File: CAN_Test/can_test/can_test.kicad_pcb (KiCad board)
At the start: 4 copper layers, 30.6 x 40.6 mm, 8 parts, among them IC1 TCAN3414DR, IC2 TCAN3414DR, J1 Conn_01x04_Pin, U1 Teensy4.0

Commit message: final thing we ordered
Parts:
- added G***: LOGO, footprints:Logo_Small, B.Cu at (41.8, 35.2)
- added G***: LOGO, footprints:bird, B.Cu at (57.5, 33.7)

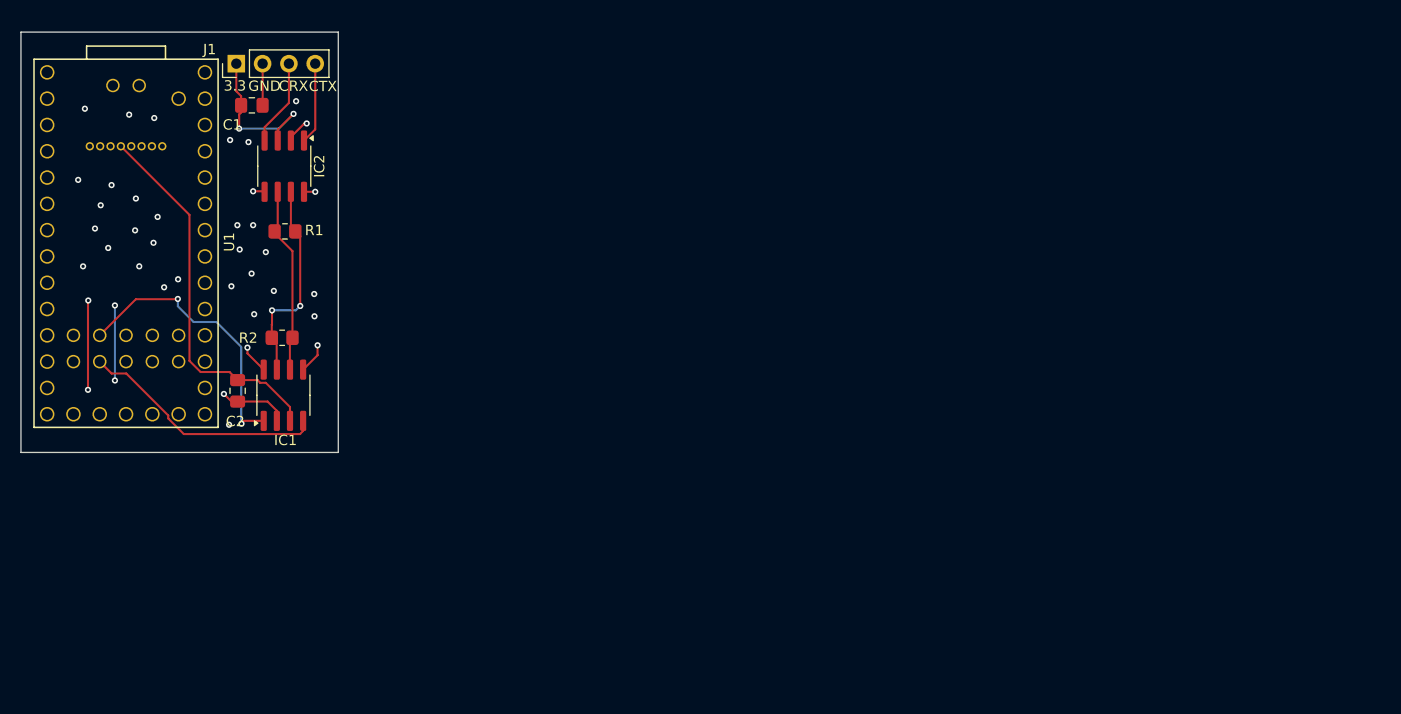
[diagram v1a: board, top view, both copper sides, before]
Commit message: update can test to teensy 41
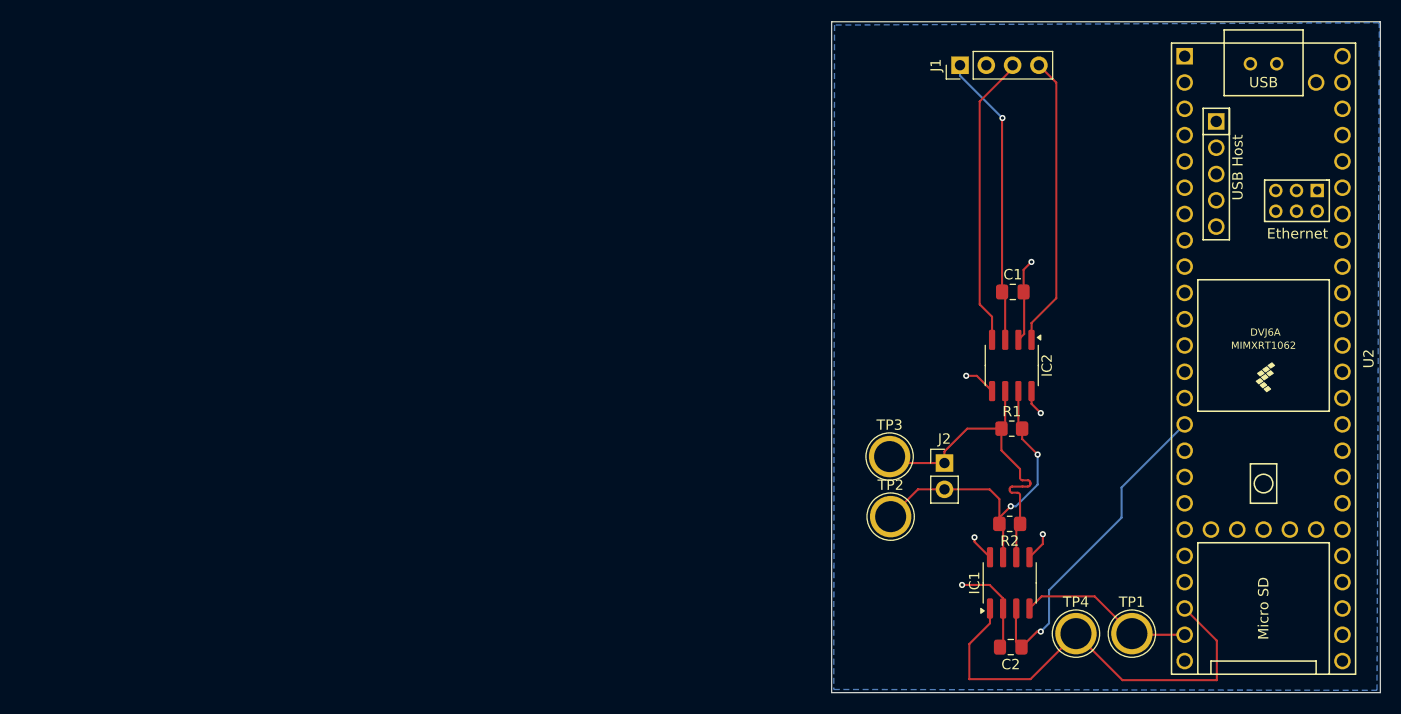
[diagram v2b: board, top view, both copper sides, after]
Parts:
- removed G***: LOGO, footprints:Logo_Small
- removed G***: LOGO, footprints:bird
- removed U1: Teensy4.0, teensy:Teensy40_SMT
- added J2: Conn_01x02_Pin, Connector_PinHeader_2.54mm:PinHeader_1x02_P2.54mm_Vertical, F.Cu at (121.3, 57.5)
- added TP1: TestPoint_Probe, TestPoint:TestPoint_Plated_Hole_D3.0mm, F.Cu at (139.4, 74.0)
- added TP2: TestPoint_Probe, TestPoint:TestPoint_Plated_Hole_D3.0mm, F.Cu at (116.1, 62.7)
- added TP3: TestPoint_Probe, TestPoint:TestPoint_Plated_Hole_D3.0mm, F.Cu at (116.0, 56.9)
- added TP4: TestPoint_Probe, TestPoint:TestPoint_Plated_Hole_D3.0mm, F.Cu at (134.0, 74.0)
- added U2: Teensy4.1, teensy:Teensy41, F.Cu at (152.1, 47.4)
- moved C2 78.7 mm to (127.7, 75.3), turned to 180 degrees
- moved C1 75.7 mm to (127.9, 41.0)
- moved IC2 72.9 mm to (127.8, 48.1)
- moved R1 72.7 mm to (127.8, 54.2)
- moved R2 72.5 mm to (127.6, 63.4)
- moved IC1 72.5 mm to (127.6, 69.1)
- moved J1 69.9 mm to (122.8, 19.1)
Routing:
- net CRX2: track 8.40 -> 28.8 mm
- net CTX2: track 7.88 -> 28.2 mm
- net CTX1: track 27.1 -> 43.5 mm, vias 2 -> 0
- net CANL: track 18.1 -> 33.5 mm
- net CANH: track 20.2 -> 33.2 mm
- net Net-(IC2-VCC): track 15.6 -> 28.4 mm, vias 2 -> 1
- net GND: track 37.0 -> 28.3 mm, vias 40 -> 6
- net CRX1: track 23.8 -> 17.0 mm
- net +3.3V: track 36.4 -> 32.2 mm, vias 0 -> 1
- added copper zone on B.Cu, net GND
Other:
- board size 30.6 x 40.6 mm -> 53 x 64.8 mm
- board text removed: "3.3"
- board text removed: "CRX"
- board text removed: "CTX"
- board text removed: "GND"

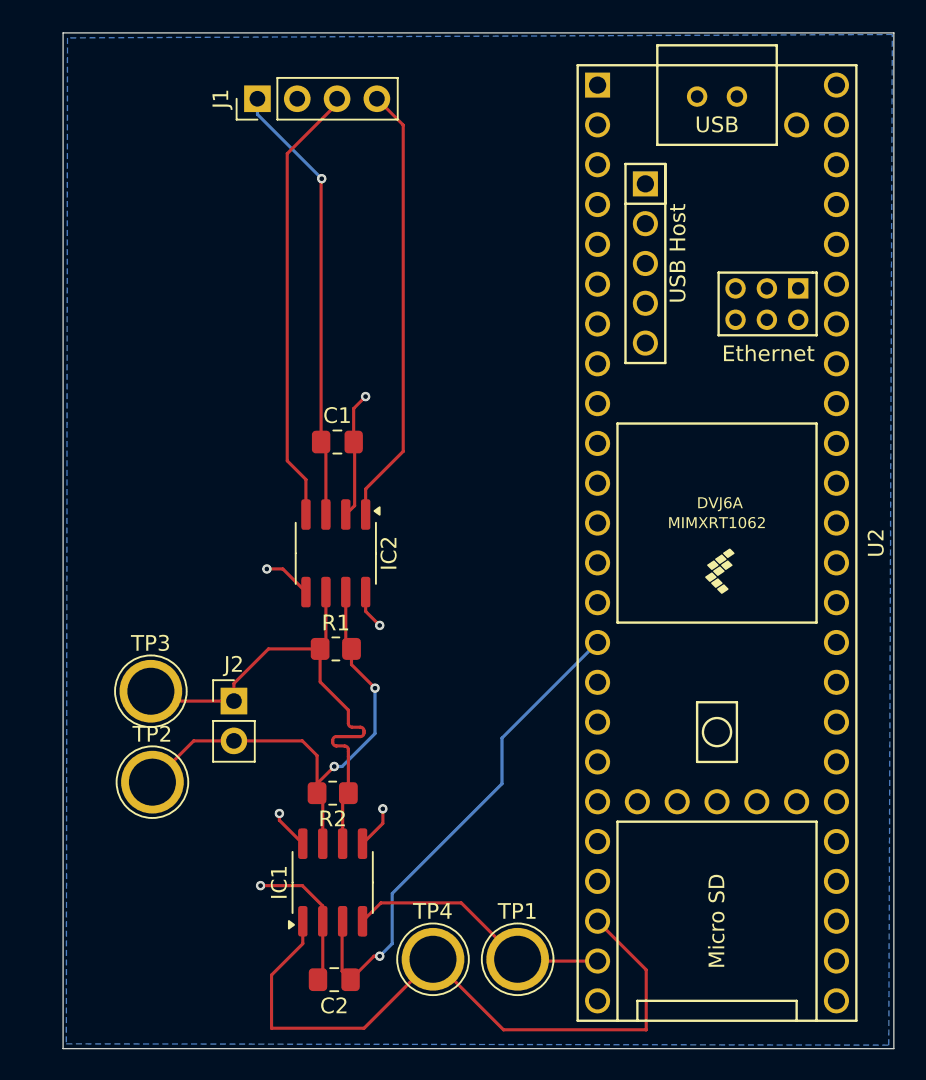
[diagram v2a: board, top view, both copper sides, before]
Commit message: make fixes sylvester reccomended
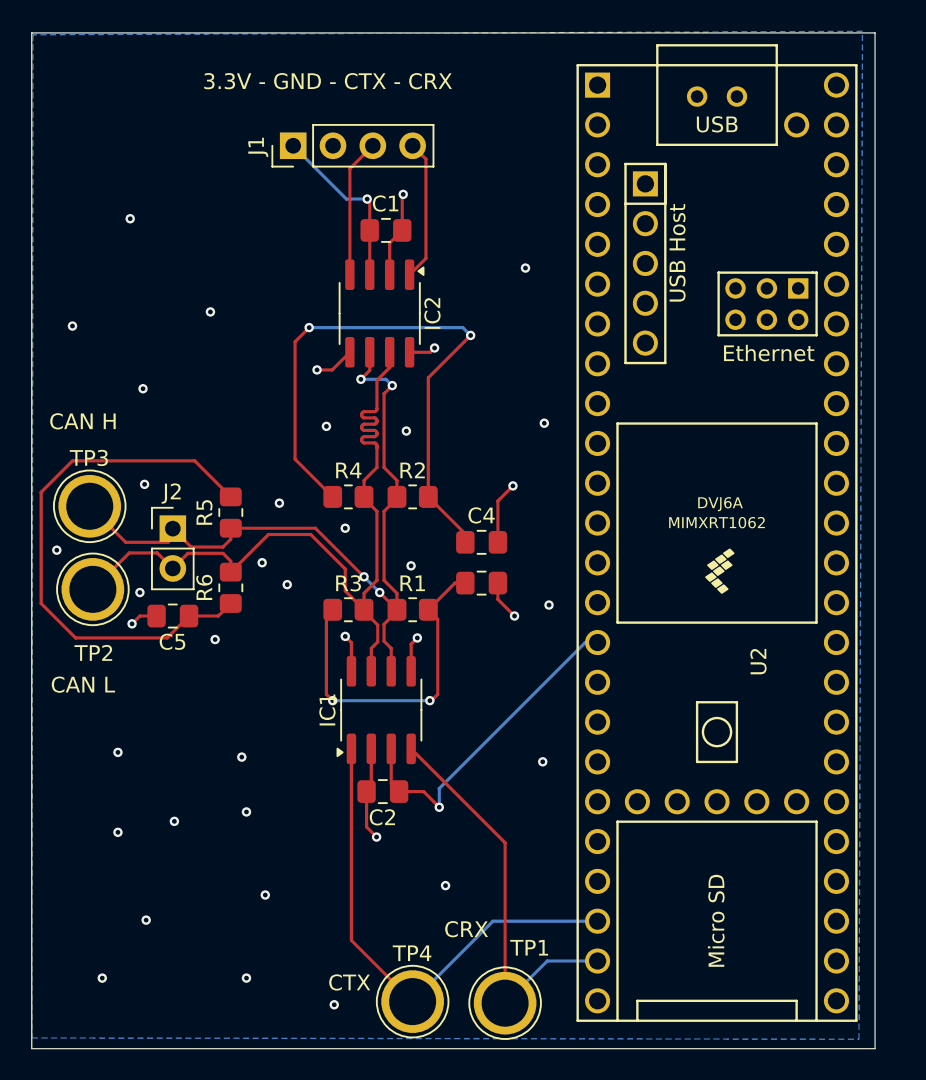
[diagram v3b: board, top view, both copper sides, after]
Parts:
- added C3: C, Capacitor_SMD:C_0805_2012Metric_Pad1.18x1.45mm_HandSolder, F.Cu at (137.1, 50.0)
- added C4: C, Capacitor_SMD:C_0805_2012Metric_Pad1.18x1.45mm_HandSolder, F.Cu at (137.1, 47.4)
- added C5: C, Capacitor_SMD:C_0805_2012Metric_Pad1.18x1.45mm_HandSolder, F.Cu at (117.4, 52.1)
- added R3: 60, Resistor_SMD:R_0805_2012Metric_Pad1.20x1.40mm_HandSolder, F.Cu at (128.6, 51.7)
- added R4: 60, Resistor_SMD:R_0805_2012Metric_Pad1.20x1.40mm_HandSolder, F.Cu at (128.6, 44.5)
- added R5: 60, Resistor_SMD:R_0805_2012Metric_Pad1.20x1.40mm_HandSolder, F.Cu at (121.1, 45.5)
- added R6: 60, Resistor_SMD:R_0805_2012Metric_Pad1.20x1.40mm_HandSolder, F.Cu at (121.1, 50.3)
- R1, R2: value 120Ohm -> 60
- moved R2 19.6 mm to (132.7, 44.5), turned to 0 degrees
- moved IC2 15.6 mm to (130.6, 32.8)
- moved C1 13.9 mm to (131.0, 27.5)
- moved TP2 12.9 mm to (112.3, 50.4)
- moved TP3 12.4 mm to (112.1, 45.1)
- moved C2 12.4 mm to (130.8, 63.3)
- moved J2 11.7 mm to (117.4, 46.5)
- moved IC1 11.4 mm to (130.7, 58.1)
- moved R1 5.50 mm to (132.7, 51.7)
- moved J1 3.77 mm to (125.1, 22.1)
- moved TP4 3.00 mm to (132.7, 76.7)
- moved TP1 2.91 mm to (138.6, 76.8)
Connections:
- net CANL renamed CANN
- IC1 pad 7: CANH -> CANP
- IC2 pad 7: CANH -> CANP
- J2 pad 2: CANH -> CANP
- R1 pad 2: CANH -> Net-(C3-Pad1)
- R2 pad 2: CANH -> Net-(C4-Pad1)
- TP2 pad 1: CANH -> CANP
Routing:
- net CANP: track 0.00 -> 51.1 mm
- net Net-(C4-Pad1): track 0.00 -> 38.0 mm, vias 0 -> 2
- net Net-(C5-Pad1): track 0.00 -> 34.9 mm
- net CANH: track 33.2 -> 0.00 mm, vias 2 -> 0
- net Net-(C3-Pad1): track 0.00 -> 21.7 mm, vias 0 -> 2
- net CRX2: track 28.8 -> 8.83 mm
- net CTX2: track 28.2 -> 9.01 mm
- net Net-(IC2-VCC): track 28.4 -> 11.0 mm
- net CANN: track 33.5 -> 48.0 mm, vias 0 -> 4
- net +3.3V: track 32.2 -> 21.1 mm
- net CTX1: track 43.5 -> 32.3 mm
- net CRX1: track 17.0 -> 25.7 mm
- net GND: track 28.3 -> 28.8 mm, vias 6 -> 39
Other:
- board size 53 x 64.8 mm -> 53.8 x 64.8 mm
- board text added: "3.3V - GND - CTX - CRX"
- board text added: "CAN H"
- board text added: "CAN L"
- board text added: "CRX"
- board text added: "CTX"

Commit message: cleanup pcb
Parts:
- removed C5: C, Capacitor_SMD:C_0805_2012Metric_Pad1.18x1.45mm_HandSolder
- removed R5, R6: 60, Resistor_SMD:R_0805_2012Metric_Pad1.20x1.40mm_HandSolder
- moved C4 2.94 mm to (136.6, 44.5)
- moved C3 1.77 mm to (136.6, 51.7)
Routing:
- net Net-(C5-Pad1): track 34.9 -> 0.00 mm
- net GND: track 28.8 -> 17.2 mm, vias 39 -> 37
- net Net-(C4-Pad1): track 38.0 -> 36.0 mm
- net CANP: track 51.1 -> 49.7 mm
- net Net-(C3-Pad1): track 21.7 -> 20.5 mm
- net CANN: track 48.0 -> 47.0 mm
